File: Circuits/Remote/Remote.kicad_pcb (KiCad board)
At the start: 2 copper layers, 84 x 64 mm, 31 parts, among them CN1 WRITER, CN2 CONN_4, Q1 2SK4017, SW1 WakeUp, U1 TWE_LITE_SMD, U2 STEPUPDIP3.3V, U3 ATP3011-PU, U4 HT82V739

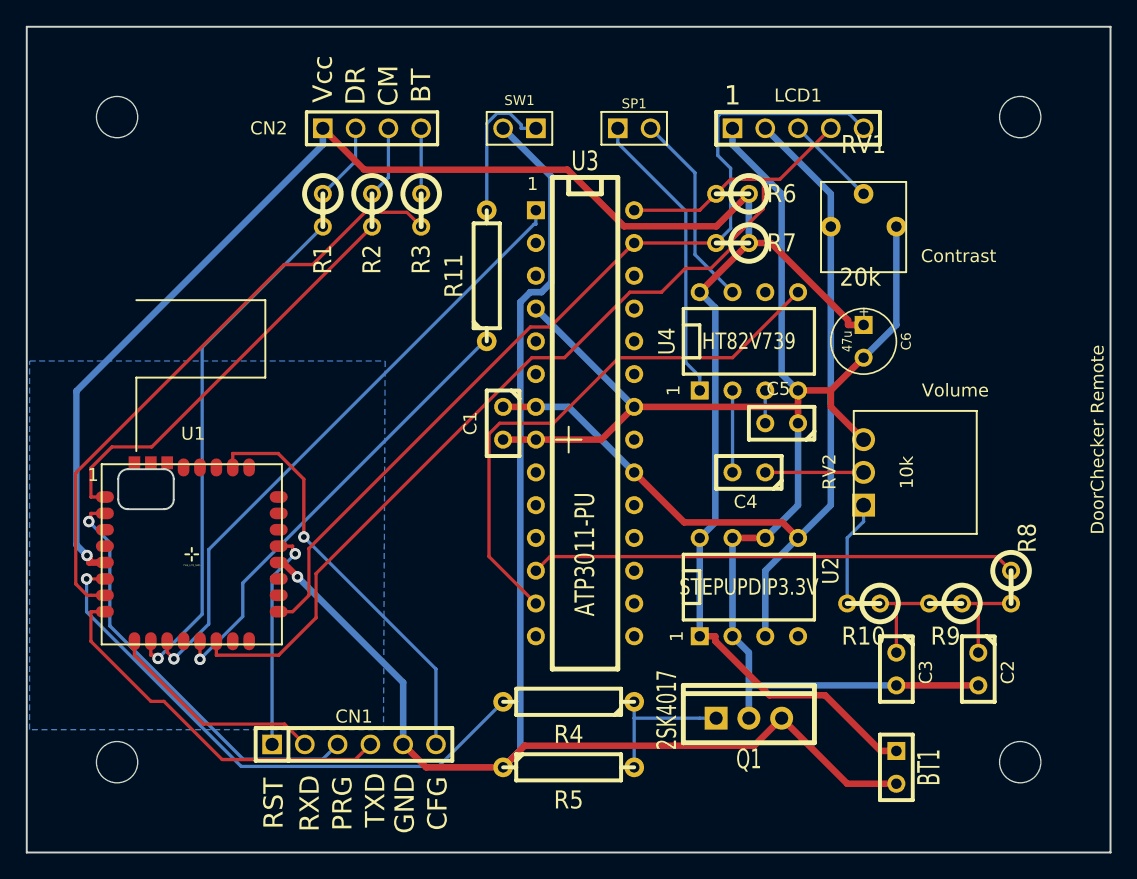
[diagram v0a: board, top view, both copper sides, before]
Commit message: Migrating to current version of KiCad.
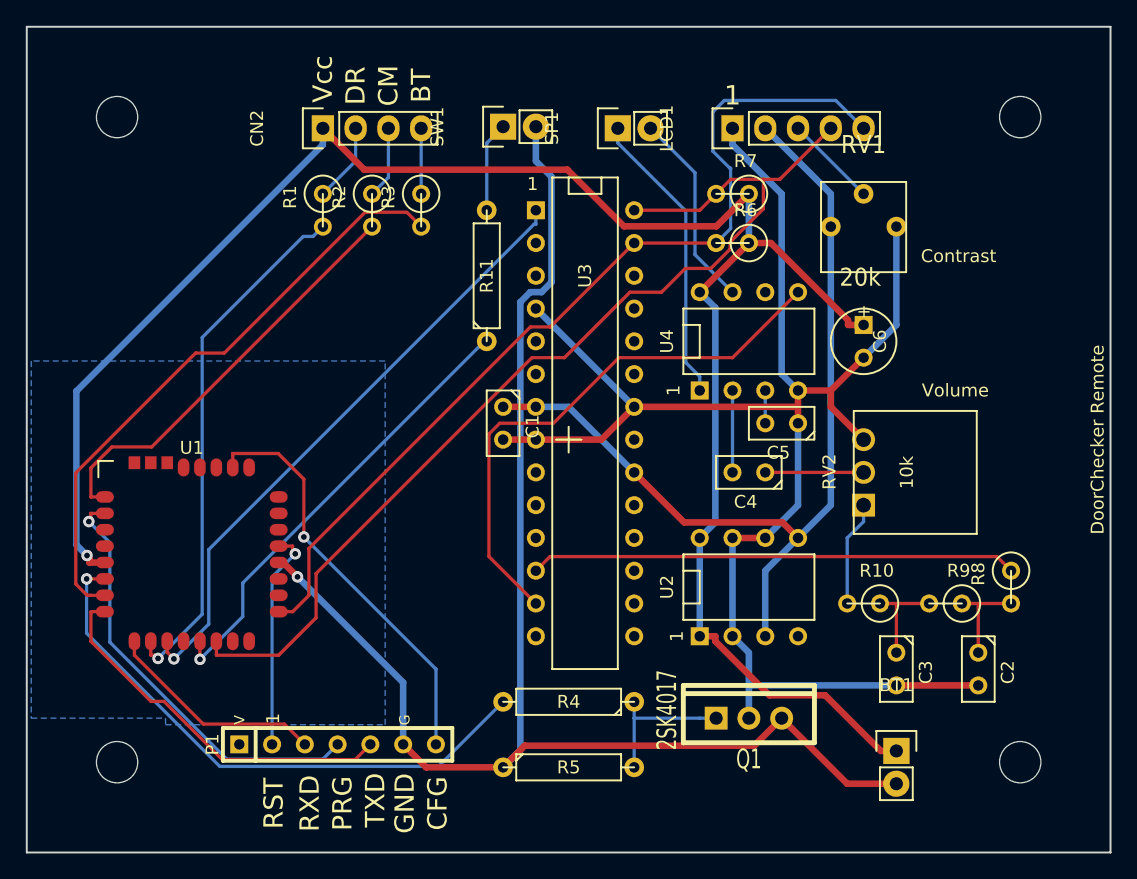
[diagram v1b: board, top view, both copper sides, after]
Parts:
- removed CN1: WRITER, PIN_ARRAY-6X1
- added P1: WRITER-VCC, favorites:WRITE-7P, F.Cu at (39.2, 69.3)
- BT1: footprint SIL-2 -> Pin_Headers:Pin_Header_Straight_1x02
- C1, C2, C3, C4, C5: footprint C1 -> Discret:C1
- C6: footprint C1V5 -> Discret:C1V5
- CN2: footprint PIN_ARRAY_4x1 -> Pin_Headers:Pin_Header_Straight_1x04
- LCD1: footprint PIN_ARRAY_5x1 -> Pin_Headers:Pin_Header_Straight_1x05
- Q1: footprint TO220_VERT_GDS -> favorites:TO220_VERT_GDS
- R1, R10, R2, R3, R6, R7, R8, R9: footprint R1 -> Discret:R1
- R11, R4, R5: footprint R4 -> Discret:R4
- RV1: footprint RV-3362P -> favorites:RV-3362P
- RV2: footprint RV-TSR-3386T -> favorites:RV-TSR-3386T
- SP1, SW1: footprint PIN_ARRAY_2X1 -> Pin_Headers:Pin_Header_Straight_1x02
- U1: footprint TWE-001L-SMD -> favorites:TWE-001L-SMD-noNTH
- U2: value STEPUPDIP3.3V -> STEPUP3.3V; footprint DIP-8__300 -> Sockets_DIP:DIP-8__300
- U3: footprint DIP-28__300 -> Sockets_DIP:DIP-28__300
- U4: footprint DIP-8__300 -> Sockets_DIP:DIP-8__300
- moved LCD1 5.08 mm to (69.8, 21.6), turned to 90 degrees
- moved CN2 3.81 mm to (38.1, 21.6), turned to 90 degrees
- moved SW1 1.28 mm to (52.1, 21.5), turned to 90 degrees
- moved BT1 1.27 mm to (82.5, 69.8), turned to 0 degrees
- moved SP1 1.27 mm to (61.0, 21.6), turned to 90 degrees
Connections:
- U1 pad 12: (no net) -> Net-(U1-Pad12)
- U1 pad 15: (no net) -> Net-(U1-Pad15)
- U1 pad 16: (no net) -> Net-(U1-Pad16)
- U1 pad 18: (no net) -> Net-(U1-Pad18)
- U1 pad 19: (no net) -> Net-(U1-Pad19)
- U1 pad 22: (no net) -> Net-(U1-Pad22)
- U1 pad 23: (no net) -> Net-(U1-Pad23)
- U1 pad 24: (no net) -> Net-(U1-Pad24)
- U1 pad 25: (no net) -> Net-(U1-Pad25)
- U1 pad 27: (no net) -> Net-(U1-Pad27)
- U1 pad 28: (no net) -> Net-(U1-Pad28)
- U1 pad 29: (no net) -> Net-(U1-Pad29)
- U1 pad 3: (no net) -> Net-(U1-Pad3)
- U1 pad 30: (no net) -> Net-(U1-Pad30)
- U1 pad 31: (no net) -> Net-(U1-Pad31)
- U1 pad 32: (no net) -> Net-(U1-Pad32)
- U1 pad 4: (no net) -> Net-(U1-Pad4)
- U2 pad 4: (no net) -> Net-(U2-Pad4)
- U3 pad 10: (no net) -> Net-(U3-Pad10)
- U3 pad 11: (no net) -> Net-(U3-Pad11)
- U3 pad 14: (no net) -> Net-(U3-Pad14)
- U3 pad 15: (no net) -> Net-(U3-Pad15)
- U3 pad 16: (no net) -> Net-(U3-Pad16)
- U3 pad 17: (no net) -> Net-(U3-Pad17)
- U3 pad 18: (no net) -> Net-(U3-Pad18)
- U3 pad 19: (no net) -> Net-(U3-Pad19)
- U3 pad 2: (no net) -> Net-(U3-Pad2)
- U3 pad 21: (no net) -> Net-(U3-Pad21)
- U3 pad 23: (no net) -> Net-(U3-Pad23)
- U3 pad 24: (no net) -> Net-(U3-Pad24)
- U3 pad 25: (no net) -> Net-(U3-Pad25)
- U3 pad 26: (no net) -> Net-(U3-Pad26)
- U3 pad 3: (no net) -> Net-(U3-Pad3)
- U3 pad 5: (no net) -> Net-(U3-Pad5)
- U3 pad 6: (no net) -> Net-(U3-Pad6)
- U3 pad 9: (no net) -> Net-(U3-Pad9)
- U4 pad 6: (no net) -> Net-(U4-Pad6)
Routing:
- net /SW: track 11.5 -> 7.00 mm
- net /SDA: track 70.4 -> 72.1 mm
- net /GND_SW: track 43.3 -> 44.3 mm
- net GND: track 114.1 -> 113.2 mm
- net /PRG: track 32.9 -> 33.7 mm

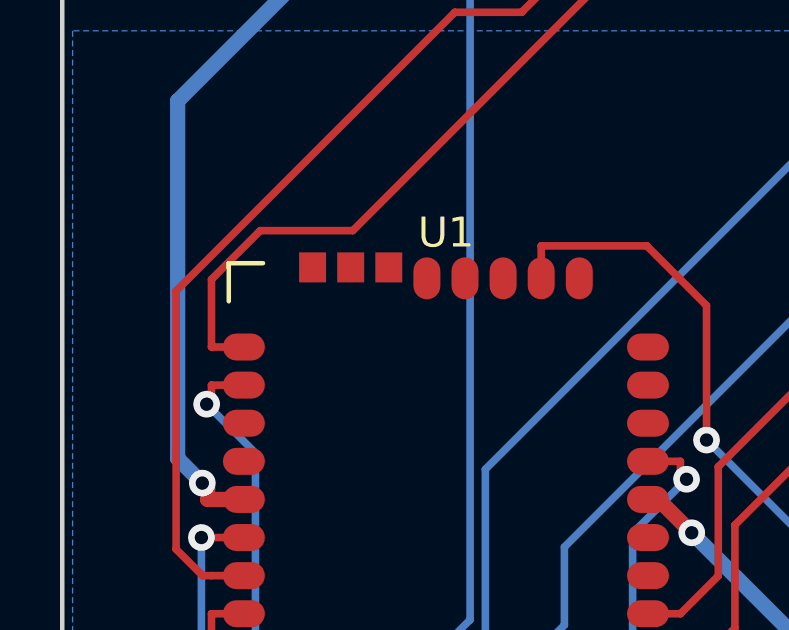
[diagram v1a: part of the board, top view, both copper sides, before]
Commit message: Changed location of 3d shapes.
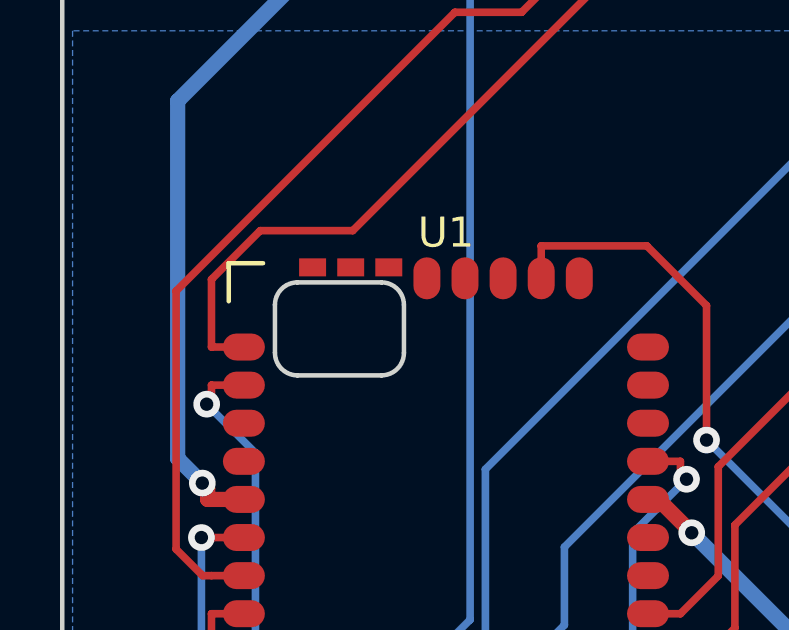
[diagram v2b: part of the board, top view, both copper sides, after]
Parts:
- U1: footprint favorites:TWE-001L-SMD-noNTH -> favorites:TWE-001L-SMD
